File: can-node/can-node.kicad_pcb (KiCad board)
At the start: 4 copper layers, 75.4 x 43.5 mm, 139 parts, among them J1 Conn_ARM_JTAG_SWD_10, J2 Conn_01x04_Pin, J3 USART1, J4 Harwin M80-5402642, J5 Harwin M80-5402642, Q1 DMP510DL-7, SW1 RESET, U1 TCAN3404-Q1, U10 TLV9101IDBVR, U11 TLV9101IDBVR, U12 TLV9101IDBVR, U13 TLV9101IDBVR, U14 TLV9101IDBVR, U15 TLV9101IDBVR, U16 TLV9101IDBVR, U17 TLV9101IDBVR, U18 TLV9101IDBVR, U19 TLV9101IDBVR, U2 STM32F105RBTx, U3 AP7375-33FDC, U4 TLV9101IDBVR, U5 TLV9101IDBVR, U6 TLV9101IDBVR, U7 TLV9101IDBVR, U8 TLV9101IDBVR, U9 TLV9101IDBVR, Y1 ECS-250-10-47Q-CES-TR

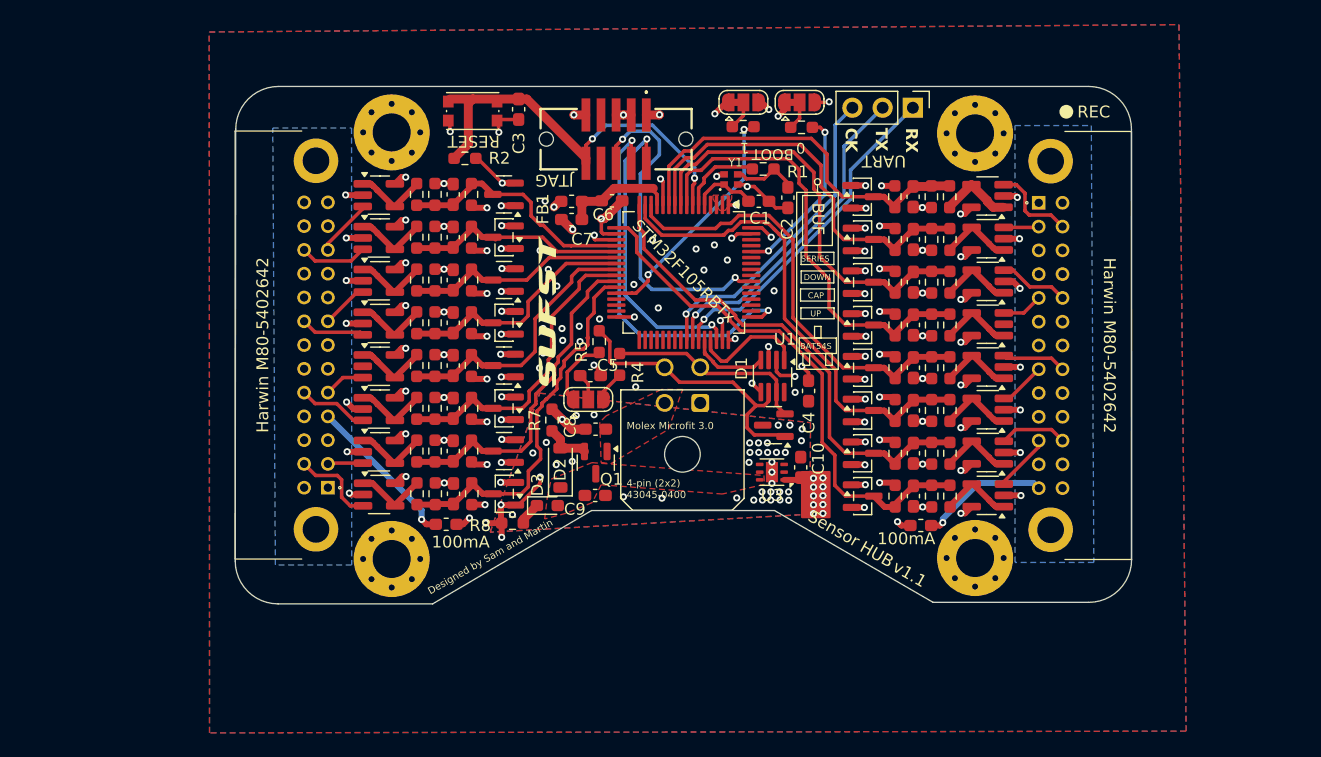
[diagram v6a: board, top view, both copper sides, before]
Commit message: Switched back to molex
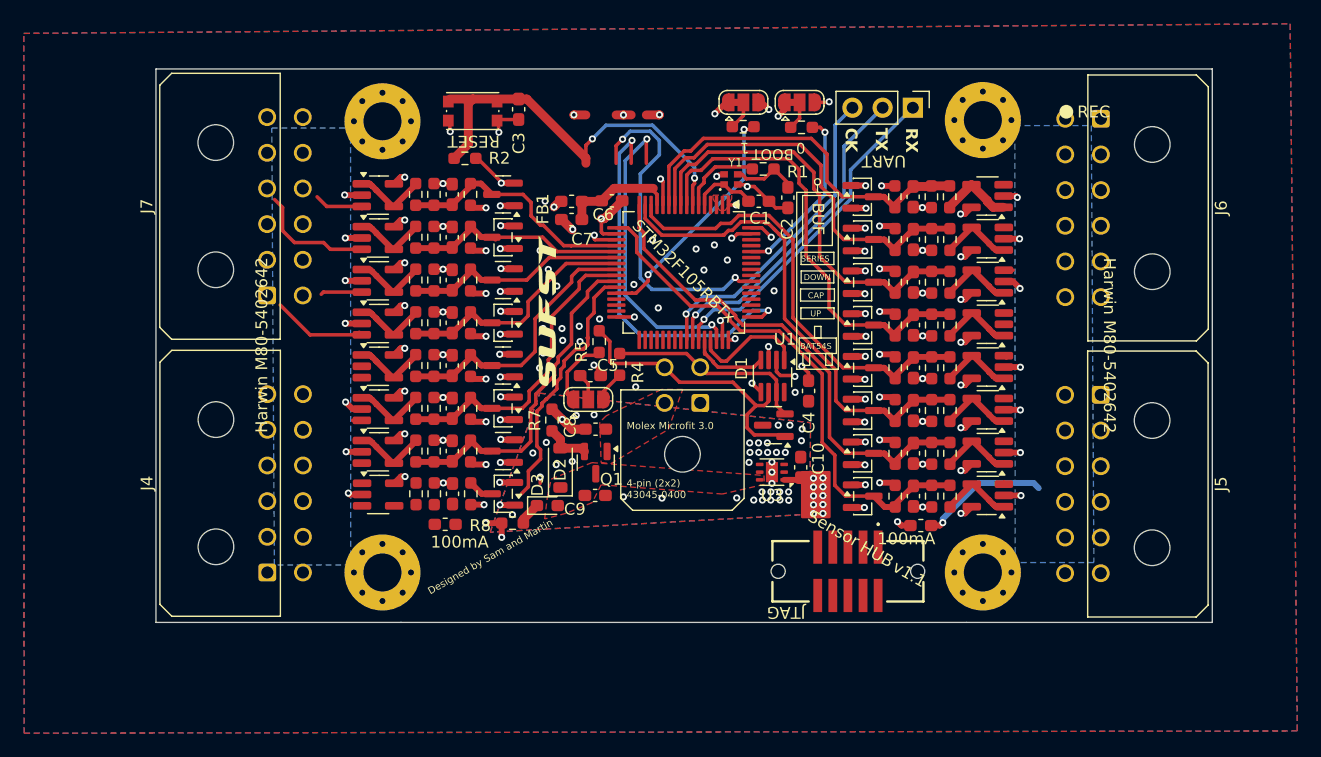
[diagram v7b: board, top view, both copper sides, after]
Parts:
- added J6: Conn_02x06_Top_Bottom, Connector_Molex:Molex_Micro-Fit_3.0_43045-1200_2x06_P3.00mm_Horizontal, F.Cu at (153.9, 117.0)
- added J7: Conn_02x06_Top_Bottom, Connector_Molex:Molex_Micro-Fit_3.0_43045-1200_2x06_P3.00mm_Horizontal, F.Cu at (83.8, 131.8)
- J4, J5: value Harwin M80-5402642 -> Conn_02x06_Top_Bottom; footprint SUFST:M80-5402642 -> Connector_Molex:Molex_Micro-Fit_3.0_43045-1200_2x06_P3.00mm_Horizontal
- moved J4 72.0 mm to (83.8, 155.2)
- moved J5 65.5 mm to (153.9, 140.2)
- moved J1 41.2 mm to (132.7, 155.1)
- moved H4 1.38 mm to (144.0, 155.2)
- moved H1 1.37 mm to (93.5, 155.2)
- moved H3 1.29 mm to (144.0, 117.1)
- moved H2 1.21 mm to (93.5, 117.2)
- moved F2 0.08 mm to (98.8, 151.1)
- moved C11 0.08 mm to (99.4, 148.5)
- moved C22 0.08 mm to (99.4, 123.3)
- moved D12 0.08 mm to (103.6, 144.9)
- moved D15 0.08 mm to (103.6, 123.3)
- moved D4 0.08 mm to (103.7, 148.5)
- moved R10 0.08 mm to (100.9, 148.5)
- moved R11 0.08 mm to (97.9, 148.5)
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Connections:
- C11 pad 1: /ADC_0_4 -> /ADC_1_4
- C12 pad 1: /ADC_0_5 -> /ADC_1_5
- C15 pad 1: /ADC_1_3 -> /ADC_1_0
- C16 pad 1: /ADC_1_2 -> /ADC_1_1
- C17 pad 1: /ADC_1_1 -> /ADC_1_2
- C18 pad 1: /ADC_1_0 -> /ADC_1_3
- C23 pad 1: /ADC_1_4 -> /ADC_0_4
- C25 pad 1: /ADC_1_5 -> /ADC_0_5
- D10 pad 3: /ADC_1_1 -> /ADC_1_2
- D11 pad 3: /ADC_1_0 -> /ADC_1_3
- D16 pad 3: /ADC_1_4 -> /ADC_0_4
- D18 pad 3: /ADC_1_5 -> /ADC_0_5
- D4 pad 3: /ADC_0_4 -> /ADC_1_4
- D5 pad 3: /ADC_0_5 -> /ADC_1_5
- D8 pad 3: /ADC_1_3 -> /ADC_1_0
- D9 pad 3: /ADC_1_2 -> /ADC_1_1
- J4 pad 1: unconnected-(J4-Pin_1-Pad1) -> /Generic ADC Input Group1/ClampedDivider20/IN
- J4 pad 10: /Generic ADC Input Group1/3V3_FUSED -> /Generic ADC Input Group1/ClampedDivider17/IN
- J4 pad 11: /Generic ADC Input Group1/ClampedDivider23/IN -> GND
- J4 pad 12: GND -> /Generic ADC Input Group1/3V3_FUSED
- J4 pad 2: /Generic ADC Input Group1/ClampedDivider20/IN -> GND
- J4 pad 3: GND -> /Generic ADC Input Group1/3V3_FUSED
- J4 pad 4: /Generic ADC Input Group1/3V3_FUSED -> /Generic ADC Input Group1/ClampedDivider21/IN
- J4 pad 5: /Generic ADC Input Group1/ClampedDivider21/IN -> GND
- J4 pad 6: GND -> /Generic ADC Input Group1/3V3_FUSED
- J4 pad 7: /Generic ADC Input Group1/3V3_FUSED -> /Generic ADC Input Group1/ClampedDivider16/IN
- J4 pad 8: /Generic ADC Input Group1/ClampedDivider22/IN -> GND
- J4 pad 9: GND -> /Generic ADC Input Group1/3V3_FUSED
- J5 pad 1: unconnected-(J5-Pin_1-Pad1) -> /Generic ADC Input Group1/ClampedDivider22/IN
- J5 pad 10: /Generic ADC Input Group/3V3_FUSED -> /Generic ADC Input Group1/ClampedDivider19/IN
- J5 pad 11: /Generic ADC Input Group/ClampedDivider23/IN -> GND
- J5 pad 12: GND -> /Generic ADC Input Group1/3V3_FUSED
- J5 pad 2: /Generic ADC Input Group/ClampedDivider20/IN -> GND
- J5 pad 3: GND -> /Generic ADC Input Group1/3V3_FUSED
- J5 pad 4: /Generic ADC Input Group/3V3_FUSED -> /Generic ADC Input Group1/ClampedDivider23/IN
- J5 pad 5: /Generic ADC Input Group/ClampedDivider21/IN -> GND
- J5 pad 6: GND -> /Generic ADC Input Group1/3V3_FUSED
- J5 pad 7: /Generic ADC Input Group/3V3_FUSED -> /Generic ADC Input Group1/ClampedDivider18/IN
- J5 pad 8: /Generic ADC Input Group/ClampedDivider22/IN -> GND
- J5 pad 9: GND -> /Generic ADC Input Group1/3V3_FUSED
- R10 pad 1: /ADC_0_4 -> /ADC_1_4
- R11 pad 2: /ADC_0_4 -> /ADC_1_4
- R12 pad 1: /ADC_0_5 -> /ADC_1_5
- R13 pad 1: /ADC_0_5 -> /ADC_1_5
- R14 pad 2: /ADC_0_5 -> /ADC_1_5
- R21 pad 1: /ADC_1_3 -> /ADC_1_0
- R21 pad 2: Net-(U11--) -> Net-(U8--)
- R22 pad 1: /ADC_1_3 -> /ADC_1_0
- R23 pad 2: /ADC_1_3 -> /ADC_1_0
- R24 pad 1: /ADC_1_2 -> /ADC_1_1
- R24 pad 2: Net-(U10--) -> Net-(U9--)
- R25 pad 1: /ADC_1_2 -> /ADC_1_1
- R26 pad 2: /ADC_1_2 -> /ADC_1_1
- R27 pad 1: /ADC_1_1 -> /ADC_1_2
- R27 pad 2: Net-(U9--) -> Net-(U10--)
- R28 pad 1: /ADC_1_1 -> /ADC_1_2
- R29 pad 2: /ADC_1_1 -> /ADC_1_2
- R30 pad 1: /ADC_1_0 -> /ADC_1_3
- R30 pad 2: Net-(U8--) -> Net-(U11--)
- R31 pad 1: /ADC_1_0 -> /ADC_1_3
- R32 pad 2: /ADC_1_0 -> /ADC_1_3
- R45 pad 1: /ADC_1_4 -> /ADC_0_4
- R46 pad 1: /ADC_1_4 -> /ADC_0_4
- R47 pad 2: /ADC_1_4 -> /ADC_0_4
- R51 pad 1: /ADC_1_5 -> /ADC_0_5
- R52 pad 1: /ADC_1_5 -> /ADC_0_5
- R53 pad 2: /ADC_1_5 -> /ADC_0_5
- R9 pad 1: /ADC_0_4 -> /ADC_1_4
- U16 pad 3: /Generic ADC Input Group1/ClampedDivider16/IN -> /Generic ADC Input Group/ClampedDivider16/IN
- U18 pad 3: /Generic ADC Input Group1/ClampedDivider17/IN -> /Generic ADC Input Group/ClampedDivider17/IN
- U4 pad 3: /Generic ADC Input Group/ClampedDivider16/IN -> /Generic ADC Input Group1/ClampedDivider16/IN
- U5 pad 3: /Generic ADC Input Group/ClampedDivider17/IN -> /Generic ADC Input Group1/ClampedDivider17/IN
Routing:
- net /Generic ADC Input Group/3V3_FUSED: track 13.3 -> 0.00 mm, vias 1 -> 0
- net /ADC_0_4: track 31.7 -> 24.1 mm
- net /Generic ADC Input Group1/ClampedDivider16/IN: track 6.72 -> 0.00 mm
- net /Generic ADC Input Group/ClampedDivider16/IN: track 6.72 -> 0.00 mm
- net Net-(U4--): track 6.17 -> 0.00 mm
- net /Generic ADC Input Group1/ClampedDivider19/IN: track 5.72 -> 0.00 mm
- net /Generic ADC Input Group1/ClampedDivider17/IN: track 5.91 -> 0.78 mm
- net /Generic ADC Input Group/ClampedDivider17/IN: track 5.91 -> 0.78 mm
- net /Generic ADC Input Group1/ClampedDivider18/IN: track 5.41 -> 0.30 mm
- net /Generic ADC Input Group1/ClampedDivider23/IN: track 4.87 -> 0.19 mm
- net /Generic ADC Input Group/ClampedDivider19/IN: track 5.72 -> 10.2 mm
- net GND: track 103.8 -> 99.7 mm
- net /Generic ADC Input Group1/ClampedDivider22/IN: track 3.47 -> 0.00 mm
- net /Generic ADC Input Group/ClampedDivider21/IN: track 3.46 -> 0.00 mm
- net /Generic ADC Input Group1/ClampedDivider21/IN: track 3.46 -> 0.00 mm
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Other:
- board size 75.4 x 43.5 mm -> 88.9 x 46.5 mm
